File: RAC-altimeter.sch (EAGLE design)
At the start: 29 parts, among them J3 CORTEX_DEBUG_SMD, U1 MAX32660GTP+, U2 BMI088, U3 BMP388, U5 W25N01GVZEIG_TR, Y1 32.768kHz

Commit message: Reordered component numbers
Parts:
- removed C10: 0.1uF, SparkFun-Capacitors:0.1UF-0603-25V-(+80/-20%)
- removed R7: 470, SparkFun-Resistors:470OHM-0603-1/10W-1%
- added C5: 1.0uF, SparkFun-Capacitors:1.0UF-0603-16V-10%
- added R6: 10k, SparkFun-Resistors:10KOHM-0603-1/10W-1%
- C7: value 10uF -> 0.1uF; device SparkFun-Capacitors:10UF-0603-6.3V-20% -> SparkFun-Capacitors:0.1UF-0603-25V-(+80/-20%)
- C8: value 1.0uF -> 10uF; device SparkFun-Capacitors:1.0UF-0603-16V-10% -> SparkFun-Capacitors:10UF-0603-6.3V-20%
- R3: value 10k -> 4.7k; device SparkFun-Resistors:10KOHM-0603-1/10W-1% -> SparkFun-Resistors:4.7KOHM-0603-1/10W-1%
- R5: value 4.7k -> 470; device SparkFun-Resistors:4.7KOHM-0603-1/10W-1% -> SparkFun-Resistors:470OHM-0603-1/10W-1%
- renumbered C9 to C6
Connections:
- net !RSTN: now also C7.1; no longer C10.1
- net BMP_CS: now also R6.1; no longer R3.1
- net GND: now also C5.2, R5.2; no longer C10.2, R7.2
- net I2C1_SCL: now also R3.1; no longer R4.1
- net I2C1_SDA: now also R4.1; no longer R5.1
- net LED_CATH: now also R5.1; no longer R7.1
- net VCC: now also C5.1, R6.2; no longer C7.1, R5.2
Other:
- moved on the sheet: C7, C8, R3, R4, R5

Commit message: Fixed two more component numbers and added 22uF bulk decoupling
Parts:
- added C9: 22uF, SparkFun-Capacitors:22UF-1210-16V-20%
- renumbered S2 to S1, U5 to U4
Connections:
- net GND: now also C9.2
- net VCC: now also C9.1
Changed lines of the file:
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@@
 <part name="GND11" library="SparkFun-PowerSymbols" deviceset="GND" device=""/>
 <part name="SUPPLY11" library="SparkFun-PowerSymbols" deviceset="VCC" device=""/>
-<part name="S2" library="SparkFun-Switches" deviceset="MOMENTARY-SWITCH-SPST-2" device="-SMD-4.6X2.8MM"/>
+<part name="S1" library="SparkFun-Switches" deviceset="MOMENTARY-SWITCH-SPST-2" device="-SMD-4.6X2.8MM"/>
 <part name="GND20" library="SparkFun-PowerSymbols" deviceset="GND" device=""/>
 <part name="SUPPLY15" library="SparkFun-PowerSymbols" deviceset="VCC" device=""/>
@@
 <part name="H3" library="holes" library_urn="urn:adsk.eagle:library:237" deviceset="MOUNT-HOLE" device="2.8" package3d_urn="urn:adsk.eagle:package:14271/1"/>
 <part name="H4" library="holes" library_urn="urn:adsk.eagle:library:237" deviceset="MOUNT-HOLE" device="2.8" package3d_urn="urn:adsk.eagle:package:14271/1"/>
-<part name="U5" library="RAC-Altimeter" deviceset="W25N01GVZEIG_TR" device=""/>
+<part name="U4" library="RAC-Altimeter" deviceset="W25N01GVZEIG_TR" device=""/>
 <part name="GND23" library="SparkFun-PowerSymbols" deviceset="GND" device=""/>
 <part name="SUPPLY16" library="SparkFun-PowerSymbols" deviceset="VCC" device=""/>
@@
 <part name="SUPPLY7" library="SparkFun-PowerSymbols" deviceset="VCC" device=""/>
 <part name="GND7" library="SparkFun-PowerSymbols" deviceset="GND" device=""/>
+<part name="C9" library="SparkFun-Capacitors" library_urn="urn:adsk.eagle:library:510" deviceset="22UF" device="-1210-16V-20%" package3d_urn="urn:adsk.eagle:package:37436/1" value="22uF"/>
 </parts>
 <sheets>
@@
 <attribute name="VALUE" x="-88.9" y="178.054" size="1.778" layer="96" align="bottom-center"/>
 </instance>
-<instance part="S2" gate="G$1" x="-86.36" y="58.42" smashed="yes">
+<instance part="S1" gate="G$1" x="-86.36" y="58.42" smashed="yes">
 <attribute name="NAME" x="-86.36" y="63.246" size="1.778" layer="95" font="vector" align="bottom-center"/>
 <attribute name="VALUE" x="-86.36" y="55.626" size="1.778" layer="96" font="vector" align="top-center"/>
@@
 <attribute name="NAME" x="-74.168" y="33.6042" size="1.778" layer="95"/>
 </instance>
-<instance part="U5" gate="G$1" x="38.1" y="137.16" smashed="yes" rot="MR0">
+<instance part="U4" gate="G$1" x="38.1" y="137.16" smashed="yes" rot="MR0">
 <attribute name="NAME" x="21.59" y="114.3" size="1.778" layer="95" align="center-left"/>
 <attribute name="VALUE" x="21.59" y="111.76" size="1.778" layer="96" align="center-left"/>
@@
 <instance part="GND7" gate="1" x="-124.46" y="109.22" smashed="yes" rot="MR0">
 <attribute name="VALUE" x="-124.46" y="108.966" size="1.778" layer="96" rot="MR0" align="top-center"/>
+</instance>
+<instance part="C9" gate="G$1" x="-43.18" y="124.46" smashed="yes">
+<attribute name="NAME" x="-41.656" y="127.381" size="1.778" layer="95" font="vector"/>
+<attribute name="VALUE" x="-41.656" y="122.301" size="1.778" layer="96" font="vector"/>
 </instance>
 </instances>
@@
 </segment>
 <segment>
-<pinref part="U5" gate="G$1" pin="CLK"/>
+<pinref part="U4" gate="G$1" pin="CLK"/>
 <wire x1="38.1" y1="132.08" x2="50.8" y2="132.08" width="0.1524" layer="91"/>
 <label x="50.8" y="132.08" size="1.778" layer="95"/>
@@
 </segment>
 <segment>
-<pinref part="U5" gate="G$1" pin="DO_(IO1)"/>
+<pinref part="U4" gate="G$1" pin="DO_(IO1)"/>
 <wire x1="-5.08" y1="137.16" x2="-10.16" y2="137.16" width="0.1524" layer="91"/>
 <label x="-10.16" y="137.16" size="1.778" layer="95" rot="MR0"/>
@@
 </segment>
 <segment>
-<pinref part="U5" gate="G$1" pin="DI_(IO0)"/>
+<pinref part="U4" gate="G$1" pin="DI_(IO0)"/>
 <wire x1="38.1" y1="137.16" x2="50.8" y2="137.16" width="0.1524" layer="91"/>
 <label x="50.8" y="137.16" size="1.778" layer="95"/>
@@
 </segment>
 <segment>
-<pinref part="U5" gate="G$1" pin="!CS"/>
+<pinref part="U4" gate="G$1" pin="!CS"/>
 <wire x1="38.1" y1="134.62" x2="50.8" y2="134.62" width="0.1524" layer="91"/>
 <label x="50.8" y="134.62" size="1.778" layer="95"/>
@@
 </segment>
 <segment>
-<pinref part="S2" gate="G$1" pin="3"/>
-<pinref part="S2" gate="G$1" pin="4"/>
+<pinref part="S1" gate="G$1" pin="3"/>
+<pinref part="S1" gate="G$1" pin="4"/>
 <wire x1="-81.28" y1="58.42" x2="-81.28" y2="55.88" width="0.1524" layer="91"/>
 <wire x1="-81.28" y1="58.42" x2="-76.2" y2="58.42" width="0.1524" layer="91"/>
@@
 </segment>
 <segment>
-<pinref part="U5" gate="G$1" pin="EP"/>
-<pinref part="U5" gate="G$1" pin="GND"/>
+<pinref part="U4" gate="G$1" pin="EP"/>
+<pinref part="U4" gate="G$1" pin="GND"/>
 <wire x1="15.24" y1="111.76" x2="17.78" y2="111.76" width="0.1524" layer="91"/>
 <pinref part="GND23" gate="1" pin="GND"/>
@@
 <pinref part="J1" gate="G$1" pin="1"/>
 <wire x1="-78.74" y1="124.46" x2="-53.34" y2="124.46" width="0.1524" layer="91"/>
-<wire x1="-53.34" y1="124.46" x2="-53.34" y2="116.84" width="0.1524" layer="91"/>
+<wire x1="-53.34" y1="124.46" x2="-53.34" y2="119.38" width="0.1524" layer="91"/>
 <pinref part="GND6" gate="1" pin="GND"/>
+<pinref part="C9" gate="G$1" pin="2"/>
+<wire x1="-53.34" y1="119.38" x2="-53.34" y2="116.84" width="0.1524" layer="91"/>
+<wire x1="-43.18" y1="121.92" x2="-43.18" y2="119.38" width="0.1524" layer="91"/>
+<wire x1="-43.18" y1="119.38" x2="-53.34" y2="119.38" width="0.1524" layer="91"/>
+<junction x="-53.34" y="119.38"/>
 </segment>
 <segment>
@@
 <segment>
 <pinref part="SUPPLY16" gate="G$1" pin="VCC"/>
-<pinref part="U5" gate="G$1" pin="VCC"/>
+<pinref part="U4" gate="G$1" pin="VCC"/>
 <wire x1="17.78" y1="165.1" x2="17.78" y2="157.48" width="0.1524" layer="91"/>
 <pinref part="C8" gate="G$1" pin="1"/>
@@
 </segment>
 <segment>
-<pinref part="U5" gate="G$1" pin="!WP_(IO2)"/>
+<pinref part="U4" gate="G$1" pin="!WP_(IO2)"/>
 <wire x1="38.1" y1="129.54" x2="40.64" y2="129.54" width="0.1524" layer="91"/>
 <wire x1="40.64" y1="129.54" x2="40.64" y2="139.7" width="0.1524" layer="91"/>
 <pinref part="SUPPLY17" gate="G$1" pin="VCC"/>
-<pinref part="U5" gate="G$1" pin="!HOLD_(IO3)"/>
+<pinref part="U4" gate="G$1" pin="!HOLD_(IO3)"/>
 <wire x1="38.1" y1="127" x2="40.64" y2="127" width="0.1524" layer="91"/>
 <wire x1="40.64" y1="127" x2="40.64" y2="129.54" width="0.1524" layer="91"/>
@@
 <pinref part="J1" gate="G$1" pin="2"/>
 <wire x1="-78.74" y1="127" x2="-53.34" y2="127" width="0.1524" layer="91"/>
-<wire x1="-53.34" y1="127" x2="-53.34" y2="134.62" width="0.1524" layer="91"/>
+<wire x1="-53.34" y1="127" x2="-53.34" y2="132.08" width="0.1524" layer="91"/>
 <pinref part="SUPPLY6" gate="G$1" pin="VCC"/>
+<pinref part="C9" gate="G$1" pin="1"/>
+<wire x1="-53.34" y1="132.08" x2="-53.34" y2="134.62" width="0.1524" layer="91"/>
+<wire x1="-43.18" y1="129.54" x2="-43.18" y2="132.08" width="0.1524" layer="91"/>
+<wire x1="-43.18" y1="132.08" x2="-53.34" y2="132.08" width="0.1524" layer="91"/>
+<junction x="-53.34" y="132.08"/>
 </segment>
 <segment>
@@
 </segment>
 <segment>
-<pinref part="S2" gate="G$1" pin="1"/>
-<pinref part="S2" gate="G$1" pin="2"/>
+<pinref part="S1" gate="G$1" pin="1"/>
+<pinref part="S1" gate="G$1" pin="2"/>
 <wire x1="-91.44" y1="58.42" x2="-91.44" y2="55.88" width="0.1524" layer="91"/>
 <wire x1="-91.44" y1="58.42" x2="-96.52" y2="58.42" width="0.1524" layer="91"/>

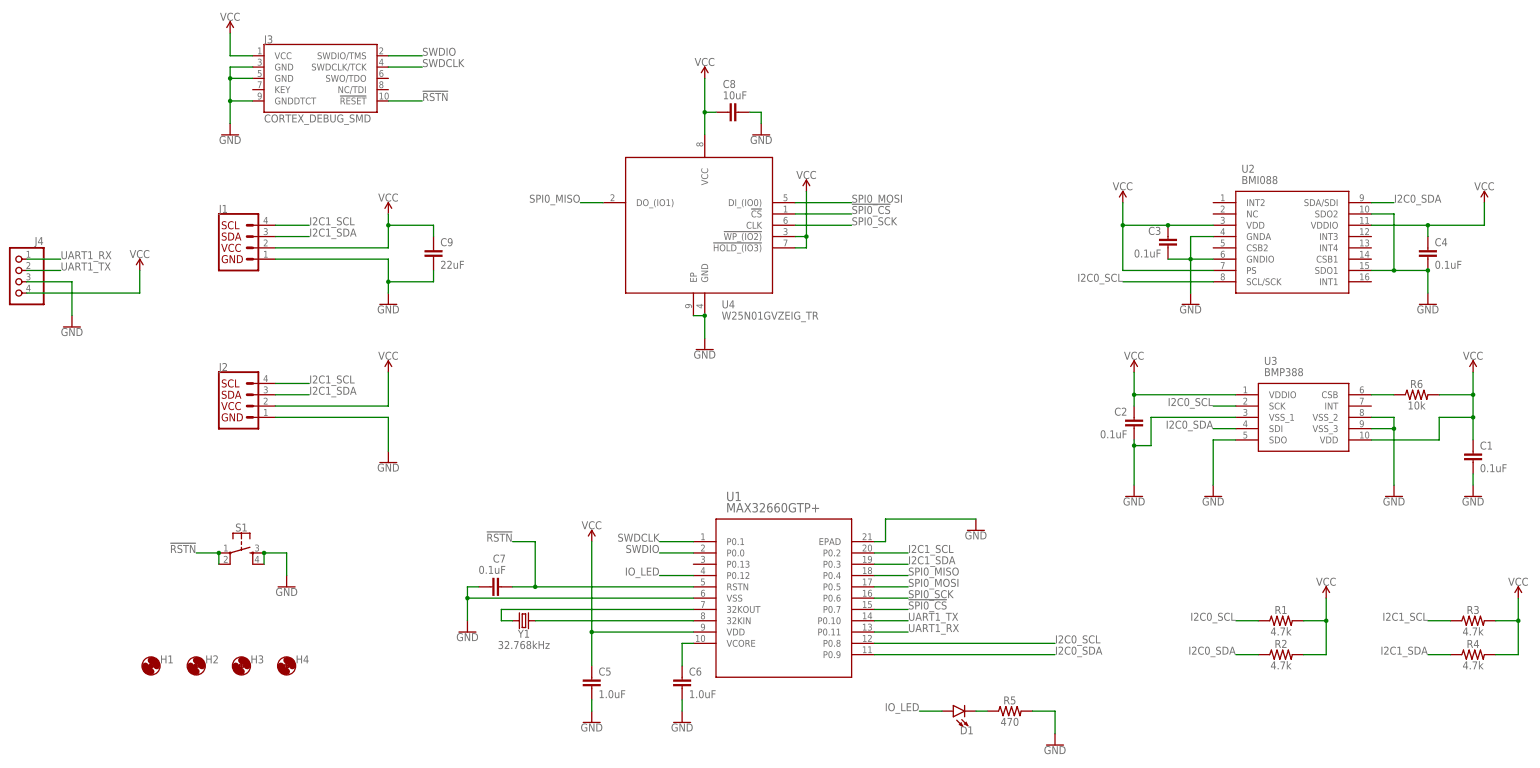
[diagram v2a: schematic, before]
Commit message: Swapped I2C0 and I2C1 bus connections for better routing
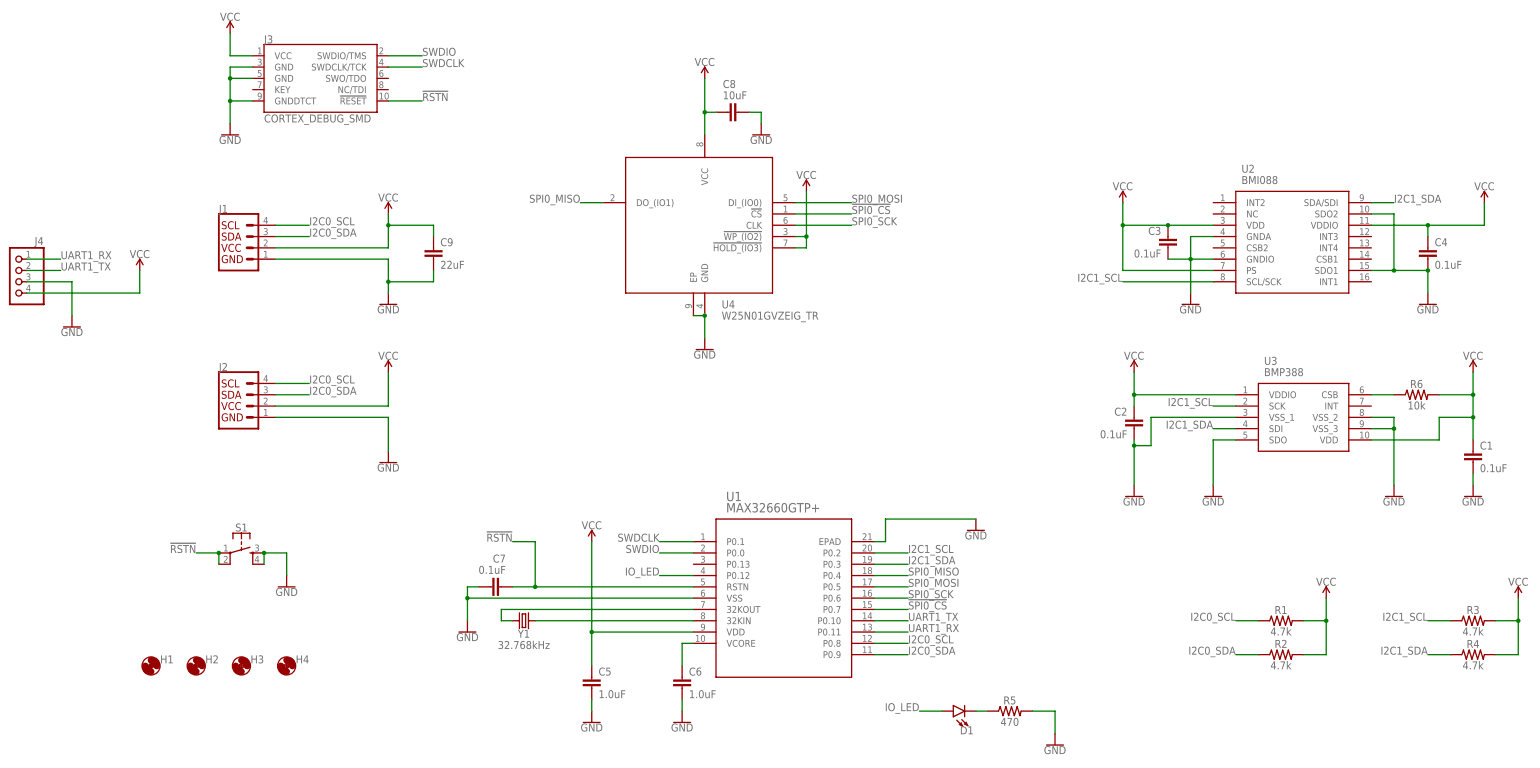
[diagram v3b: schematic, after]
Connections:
- net I2C0_SCL: now also J1.4, J2.4; no longer U2.SCL/SCK, U3.SCK
- net I2C0_SDA: now also J1.3, J2.3; no longer U2.SDA/SDI, U3.SDI
- net I2C1_SCL: now also U2.SCL/SCK, U3.SCK; no longer J1.4, J2.4
- net I2C1_SDA: now also U2.SDA/SDI, U3.SDI; no longer J1.3, J2.3
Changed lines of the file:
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@@
 <net name="I2C0_SCL" class="0">
 <segment>
-<pinref part="U3" gate="G$1" pin="SCK"/>
-<wire x1="137.16" y1="91.44" x2="132.08" y2="91.44" width="0.1524" layer="91"/>
-<label x="132.08" y="91.44" size="1.778" layer="95" rot="MR0"/>
-</segment>
-<segment>
-<pinref part="U2" gate="G$1" pin="SCL/SCK"/>
-<wire x1="132.08" y1="119.38" x2="111.76" y2="119.38" width="0.1524" layer="91"/>
-<label x="111.76" y="119.38" size="1.778" layer="95" rot="MR0"/>
-</segment>
-<segment>
 <pinref part="U1" gate="A" pin="P0.8"/>
-<wire x1="55.88" y1="38.1" x2="96.52" y2="38.1" width="0.1524" layer="91"/>
-<label x="96.52" y="38.1" size="1.778" layer="95"/>
+<wire x1="55.88" y1="38.1" x2="63.5" y2="38.1" width="0.1524" layer="91"/>
+<label x="63.5" y="38.1" size="1.778" layer="95"/>
 </segment>
 <segment>
@@
 <label x="137.16" y="43.18" size="1.778" layer="95" rot="MR0"/>
 </segment>
+<segment>
+<pinref part="J1" gate="G$1" pin="4"/>
+<wire x1="-78.74" y1="132.08" x2="-71.12" y2="132.08" width="0.1524" layer="91"/>
+<label x="-71.12" y="132.08" size="1.778" layer="95"/>
+</segment>
+<segment>
+<pinref part="J2" gate="G$1" pin="4"/>
+<wire x1="-78.74" y1="96.52" x2="-71.12" y2="96.52" width="0.1524" layer="91"/>
+<label x="-71.12" y="96.52" size="1.778" layer="95"/>
+</segment>
 </net>
 <net name="I2C0_SDA" class="0">
 <segment>
-<pinref part="U3" gate="G$1" pin="SDI"/>
-<wire x1="137.16" y1="86.36" x2="132.08" y2="86.36" width="0.1524" layer="91"/>
-<label x="132.08" y="86.36" size="1.778" layer="95" rot="MR0"/>
-</segment>
-<segment>
-<pinref part="U2" gate="G$1" pin="SDA/SDI"/>
-<wire x1="167.64" y1="137.16" x2="172.72" y2="137.16" width="0.1524" layer="91"/>
-<label x="172.72" y="137.16" size="1.778" layer="95"/>
-</segment>
-<segment>
 <pinref part="U1" gate="A" pin="P0.9"/>
-<wire x1="55.88" y1="35.56" x2="96.52" y2="35.56" width="0.1524" layer="91"/>
-<label x="96.52" y="35.56" size="1.778" layer="95"/>
+<wire x1="55.88" y1="35.56" x2="63.5" y2="35.56" width="0.1524" layer="91"/>
+<label x="63.5" y="35.56" size="1.778" layer="95"/>
 </segment>
 <segment>
@@
 <wire x1="142.24" y1="35.56" x2="137.16" y2="35.56" width="0.1524" layer="91"/>
 <label x="137.16" y="35.56" size="1.778" layer="95" rot="MR0"/>
+</segment>
+<segment>
+<pinref part="J1" gate="G$1" pin="3"/>
+<wire x1="-78.74" y1="129.54" x2="-71.12" y2="129.54" width="0.1524" layer="91"/>
+<label x="-71.12" y="129.54" size="1.778" layer="95"/>
+</segment>
+<segment>
+<pinref part="J2" gate="G$1" pin="3"/>
+<wire x1="-78.74" y1="93.98" x2="-71.12" y2="93.98" width="0.1524" layer="91"/>
+<label x="-71.12" y="93.98" size="1.778" layer="95"/>
 </segment>
 </net>
@@
 </segment>
 <segment>
-<pinref part="J2" gate="G$1" pin="4"/>
-<wire x1="-78.74" y1="96.52" x2="-71.12" y2="96.52" width="0.1524" layer="91"/>
-<label x="-71.12" y="96.52" size="1.778" layer="95"/>
-</segment>
-<segment>
-<pinref part="J1" gate="G$1" pin="4"/>
-<wire x1="-78.74" y1="132.08" x2="-71.12" y2="132.08" width="0.1524" layer="91"/>
-<label x="-71.12" y="132.08" size="1.778" layer="95"/>
+<pinref part="U3" gate="G$1" pin="SCK"/>
+<wire x1="137.16" y1="91.44" x2="132.08" y2="91.44" width="0.1524" layer="91"/>
+<label x="132.08" y="91.44" size="1.778" layer="95" rot="MR0"/>
+</segment>
+<segment>
+<pinref part="U2" gate="G$1" pin="SCL/SCK"/>
+<wire x1="132.08" y1="119.38" x2="111.76" y2="119.38" width="0.1524" layer="91"/>
+<label x="111.76" y="119.38" size="1.778" layer="95" rot="MR0"/>
 </segment>
 </net>
@@
 </segment>
 <segment>
-<pinref part="J2" gate="G$1" pin="3"/>
-<wire x1="-78.74" y1="93.98" x2="-71.12" y2="93.98" width="0.1524" layer="91"/>
-<label x="-71.12" y="93.98" size="1.778" layer="95"/>
-</segment>
-<segment>
-<pinref part="J1" gate="G$1" pin="3"/>
-<wire x1="-78.74" y1="129.54" x2="-71.12" y2="129.54" width="0.1524" layer="91"/>
-<label x="-71.12" y="129.54" size="1.778" layer="95"/>
-</segment>
-</net>
+<pinref part="U3" gate="G$1" pin="SDI"/>
+<wire x1="137.16" y1="86.36" x2="132.08" y2="86.36" width="0.1524" layer="91"/>
+<label x="132.08" y="86.36" size="1.778" layer="95" rot="MR0"/>
+</segment>
+<segment>
+<pinref part="U2" gate="G$1" pin="SDA/SDI"/>
+<wire x1="167.64" y1="137.16" x2="172.72" y2="137.16" width="0.1524" layer="91"/>
+<label x="172.72" y="137.16" size="1.778" layer="95"/>
+</segment>
+</net>

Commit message: Removed spare JST connector and BMP388 capacitor; redid IC placement
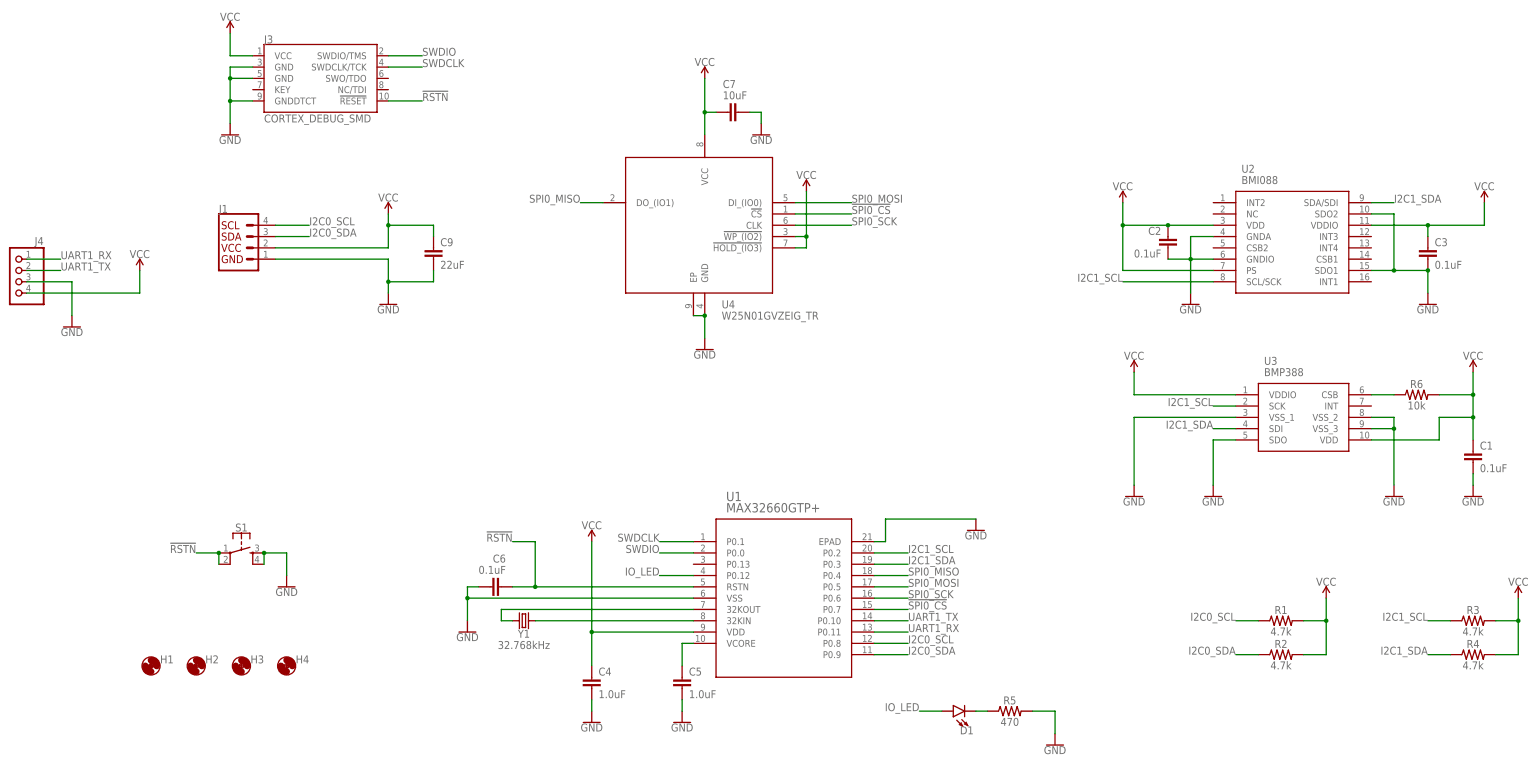
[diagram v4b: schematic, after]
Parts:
- removed C8: 10uF, SparkFun-Capacitors:10UF-0603-6.3V-20%
- removed J2: (no value), SparkFun-Connectors:QWIIC_CONNECTORJS-1MM
- C4: value 0.1uF -> 1.0uF; device SparkFun-Capacitors:0.1UF-0603-25V-(+80/-20%) -> SparkFun-Capacitors:1.0UF-0603-16V-10%
- C6: value 1.0uF -> 0.1uF; device SparkFun-Capacitors:1.0UF-0603-16V-10% -> SparkFun-Capacitors:0.1UF-0603-25V-(+80/-20%)
- C7: value 0.1uF -> 10uF; device SparkFun-Capacitors:0.1UF-0603-25V-(+80/-20%) -> SparkFun-Capacitors:10UF-0603-6.3V-20%
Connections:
- net !RSTN: now also C6.1; no longer C7.1
- net GND: now also C3.1, C4.2; no longer C3.2, C4.1, C8.2, J2.1
- net I2C0_SCL: no longer J2.4
- net I2C0_SDA: no longer J2.3
- net VCC: now also C3.2, C4.1, C7.1; no longer C3.1, C4.2, C5.1, C8.1, J2.2
- net VCORE: now also C5.1; no longer C6.1
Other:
- moved on the sheet: C2, C3, C4, C5, C6, C7
